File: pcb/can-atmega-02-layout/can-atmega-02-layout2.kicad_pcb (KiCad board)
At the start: 2 copper layers, 114 x 98 mm, 168 parts, among them J1 Screw_Terminal_01x05, J3 Conn_02x03_Odd_Even, J4 Connector_female, U1 LM1117-5.0, U2 TJA1051T, U3 MCP2515-xSO, U4 ATmega328P-A, X1 16MHz, X2 16MHz

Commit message: temp-calibrate
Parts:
- removed the C1 at (107.9, 33.1)
- removed the C1 at (69.9, 82.1)
- removed the C1 at (69.9, 33.1)
- removed the C1 at (31.9, 82.1)
- removed the C1 at (107.9, 82.1)
- removed the C1 at (31.9, 33.1)
- removed C10 (x6), C11 (x6), C5 (x6), C6 (x6): 22PF, Capacitor_SMD:C_1206_3216Metric
- removed the C2 at (71.0, 37.9)
- removed the C2 at (33.0, 37.9)
- removed the C2 at (109.0, 37.9)
- removed the C2 at (71.0, 86.9)
- removed the C2 at (109.0, 86.9)
- removed the C2 at (33.0, 86.9)
- removed the C3 at (112.3, 37.9)
- removed the C3 at (36.3, 37.9)
- removed the C3 at (112.3, 86.9)
- removed the C3 at (74.3, 37.9)
- removed the C3 at (36.3, 86.9)
- removed the C3 at (74.3, 86.9)
- removed the C4 at (77.6, 37.9)
- removed the C4 at (39.6, 37.9)
- removed the C4 at (39.6, 86.9)
- removed the C4 at (115.6, 86.9)
- removed the C4 at (115.6, 37.9)
- removed the C4 at (77.6, 86.9)
- removed C7 (x6), C9 (x6): 0.1uF, Capacitor_SMD:C_1206_3216Metric
- removed C8 (x6): 10uF/16V, Capacitor_SMD:C_1206_3216Metric
- removed the J1 at (32.6, 74.7)
- removed the J1 at (32.6, 25.7)
- removed the J1 at (70.6, 25.7)
- removed the J1 at (70.6, 74.7)
- removed the J1 at (108.6, 74.7)
- removed the J1 at (108.6, 25.7)
- removed J3 (x6): Conn_02x03_Odd_Even, Connector_IDC:IDC-Header_2x03_P2.54mm_Vertical
- removed J4 (x6): Connector_female, CAN_ATmega:Connector_female
- removed LED1 (x6): Green, LED_SMD:LED_0805_2012Metric
- removed R1 (x6): 1K, Resistor_SMD:R_0805_2012Metric
- removed R2 (x6): 10K, Resistor_SMD:R_0805_2012Metric
- removed the R3 at (75.6, 99.2)
- removed the R3 at (75.6, 50.2)
- removed the R3 at (37.6, 50.2)
- removed the R3 at (37.6, 99.2)
- removed the R3 at (113.6, 99.2)
- removed the R3 at (113.6, 50.2)
- removed the REF** at (48.5, 16.5)
- removed the REF** at (54.5, 59.5)
- removed the REF** at (54.5, 65.5)
- removed the REF** at (86.5, 108.5)
- removed the REF** at (92.5, 65.5)
- removed the REF** at (16.5, 108.5)
- removed the REF** at (16.5, 65.5)
- removed the REF** at (86.5, 16.5)
- removed the REF** at (92.5, 16.5)
- removed the REF** at (48.5, 65.5)
- removed the REF** at (124.5, 16.5)
- removed the REF** at (124.5, 65.5)
- removed the REF** at (124.5, 59.5)
- removed the REF** at (92.5, 59.5)
- removed the REF** at (48.5, 108.5)
- removed the REF** at (124.5, 108.5)
- removed the REF** at (48.5, 59.5)
- removed the REF** at (54.5, 16.5)
- removed the REF** at (92.5, 108.5)
- removed the REF** at (86.5, 65.5)
- removed the REF** at (16.5, 59.5)
- removed the REF** at (16.5, 16.5)
- removed the REF** at (86.5, 59.5)
- removed the REF** at (54.5, 108.5)
- removed the U1 at (75.8, 80.8)
- removed the U1 at (37.8, 31.8)
- removed the U1 at (113.8, 80.8)
- removed the U1 at (75.8, 31.8)
- removed the U1 at (113.8, 31.8)
- removed the U1 at (37.8, 80.8)
- removed U2 (x6): TJA1051T, Package_SO:SOIC-8_3.9x4.9mm_P1.27mm
- removed U3 (x6): MCP2515-xSO, Package_SO:SOIC-18W_7.5x11.6mm_P1.27mm
- removed U4 (x6): ATmega328P-A, Package_QFP:TQFP-32_7x7mm_P0.8mm
- removed X1 (x6), X2 (x6): 16MHz, Crystal:Crystal_HC49-4H_Vertical
- added C1: 100nF, Capacitor_SMD:C_1206_3216Metric, B.Cu at (22.0, 23.3)
- added C1: 100nF, Capacitor_SMD:C_1206_3216Metric, B.Cu at (22.0, 51.3)
- added C1: 100nF, Capacitor_SMD:C_1206_3216Metric, B.Cu at (98.0, 23.3)
- added C1: 100nF, Capacitor_SMD:C_1206_3216Metric, B.Cu at (60.0, 51.3)
- added C1: 100nF, Capacitor_SMD:C_1206_3216Metric, B.Cu at (60.0, 23.3)
- added C1: 100nF, Capacitor_SMD:C_1206_3216Metric, B.Cu at (98.0, 51.3)
- added C2: 100nF, Capacitor_SMD:C_1206_3216Metric, B.Cu at (98.0, 54.6)
- added C2: 100nF, Capacitor_SMD:C_1206_3216Metric, B.Cu at (98.0, 26.6)
- added C2: 100nF, Capacitor_SMD:C_1206_3216Metric, B.Cu at (22.0, 54.6)
- added C2: 100nF, Capacitor_SMD:C_1206_3216Metric, B.Cu at (60.0, 26.6)
- added C2: 100nF, Capacitor_SMD:C_1206_3216Metric, B.Cu at (22.0, 26.6)
- added C2: 100nF, Capacitor_SMD:C_1206_3216Metric, B.Cu at (60.0, 54.6)
- added C3: 10uF/16V, Capacitor_SMD:C_1206_3216Metric, B.Cu at (60.0, 57.6)
- added C3: 10uF/16V, Capacitor_SMD:C_1206_3216Metric, B.Cu at (22.0, 57.6)
- added C3: 10uF/16V, Capacitor_SMD:C_1206_3216Metric, B.Cu at (60.0, 29.6)
- added C3: 10uF/16V, Capacitor_SMD:C_1206_3216Metric, B.Cu at (98.0, 29.6)
- added C3: 10uF/16V, Capacitor_SMD:C_1206_3216Metric, B.Cu at (22.0, 29.6)
- added C3: 10uF/16V, Capacitor_SMD:C_1206_3216Metric, B.Cu at (98.0, 57.6)
- added C4: 100nF, Capacitor_SMD:C_1206_3216Metric, B.Cu at (119.4, 51.3)
- added C4: 100nF, Capacitor_SMD:C_1206_3216Metric, B.Cu at (81.4, 51.3)
- added C4: 100nF, Capacitor_SMD:C_1206_3216Metric, B.Cu at (81.4, 23.3)
- added C4: 100nF, Capacitor_SMD:C_1206_3216Metric, B.Cu at (43.4, 51.3)
- added C4: 100nF, Capacitor_SMD:C_1206_3216Metric, B.Cu at (119.4, 23.3)
- added C4: 100nF, Capacitor_SMD:C_1206_3216Metric, B.Cu at (43.4, 23.3)
- added J1: Connector_male, CAN_ATmega:Connector_male, F.Cu at (107.2, 23.3)
- added J1: Connector_male, CAN_ATmega:Connector_male, F.Cu at (31.2, 51.3)
- added J1: Connector_male, CAN_ATmega:Connector_male, F.Cu at (69.2, 23.3)
- added J1: Connector_male, CAN_ATmega:Connector_male, F.Cu at (107.2, 51.3)
- added J1: Connector_male, CAN_ATmega:Connector_male, F.Cu at (69.2, 51.3)
- added J1: Connector_male, CAN_ATmega:Connector_male, F.Cu at (31.2, 23.3)
- added J2: Screw_Terminal_01x03, Connector_Wago:Wago_734-163_1x03_P3.50mm_Horizontal, F.Cu at (66.8, 32.5)
- added J2: Screw_Terminal_01x03, Connector_Wago:Wago_734-163_1x03_P3.50mm_Horizontal, F.Cu at (28.8, 32.5)
- added J2: Screw_Terminal_01x03, Connector_Wago:Wago_734-163_1x03_P3.50mm_Horizontal, F.Cu at (104.8, 60.5)
- added J2: Screw_Terminal_01x03, Connector_Wago:Wago_734-163_1x03_P3.50mm_Horizontal, F.Cu at (66.8, 60.5)
- added J2: Screw_Terminal_01x03, Connector_Wago:Wago_734-163_1x03_P3.50mm_Horizontal, F.Cu at (104.8, 32.5)
- added J2: Screw_Terminal_01x03, Connector_Wago:Wago_734-163_1x03_P3.50mm_Horizontal, F.Cu at (28.8, 60.5)
- added R1_1: 1.3k, Resistor_SMD:R_0805_2012Metric, F.Cu at (101.6, 18.7)
- added R1_1: 1.3k, Resistor_SMD:R_0805_2012Metric, F.Cu at (101.6, 46.7)
- added R1_1: 1.3k, Resistor_SMD:R_0805_2012Metric, F.Cu at (63.6, 46.7)
- added R1_1: 1.3k, Resistor_SMD:R_0805_2012Metric, F.Cu at (25.6, 46.7)
- added R1_1: 1.3k, Resistor_SMD:R_0805_2012Metric, F.Cu at (25.6, 18.7)
- added R1_1: 1.3k, Resistor_SMD:R_0805_2012Metric, F.Cu at (63.6, 18.7)
- added R1_2: 2k, Resistor_SMD:R_0805_2012Metric, F.Cu at (60.8, 47.7)
- added R1_2: 2k, Resistor_SMD:R_0805_2012Metric, F.Cu at (22.8, 47.7)
- added R1_2: 2k, Resistor_SMD:R_0805_2012Metric, F.Cu at (22.8, 19.7)
- added R1_2: 2k, Resistor_SMD:R_0805_2012Metric, F.Cu at (98.8, 47.7)
- added R1_2: 2k, Resistor_SMD:R_0805_2012Metric, F.Cu at (98.8, 19.7)
- added R1_2: 2k, Resistor_SMD:R_0805_2012Metric, F.Cu at (60.8, 19.7)
- added R1_3: 10k, Resistor_SMD:R_0805_2012Metric, F.Cu at (63.6, 20.7)
- added R1_3: 10k, Resistor_SMD:R_0805_2012Metric, F.Cu at (101.6, 48.7)
- added R1_3: 10k, Resistor_SMD:R_0805_2012Metric, F.Cu at (25.6, 20.7)
- added R1_3: 10k, Resistor_SMD:R_0805_2012Metric, F.Cu at (101.6, 20.7)
- added R1_3: 10k, Resistor_SMD:R_0805_2012Metric, F.Cu at (63.6, 48.7)
- added R1_3: 10k, Resistor_SMD:R_0805_2012Metric, F.Cu at (25.6, 48.7)
- added R2_1: 330, Resistor_SMD:R_0805_2012Metric, F.Cu at (115.3, 23.0)
- added R2_1: 330, Resistor_SMD:R_0805_2012Metric, F.Cu at (77.3, 23.0)
- added R2_1: 330, Resistor_SMD:R_0805_2012Metric, F.Cu at (39.3, 23.0)
- added R2_1: 330, Resistor_SMD:R_0805_2012Metric, F.Cu at (115.3, 51.0)
- added R2_1: 330, Resistor_SMD:R_0805_2012Metric, F.Cu at (39.3, 51.0)
- added R2_1: 330, Resistor_SMD:R_0805_2012Metric, F.Cu at (77.3, 51.0)
- added R2_2: 1.3k, Resistor_SMD:R_0805_2012Metric, F.Cu at (42.1, 22.0)
- added R2_2: 1.3k, Resistor_SMD:R_0805_2012Metric, F.Cu at (80.1, 22.0)
- added R2_2: 1.3k, Resistor_SMD:R_0805_2012Metric, F.Cu at (118.1, 22.0)
- added R2_2: 1.3k, Resistor_SMD:R_0805_2012Metric, F.Cu at (80.1, 50.0)
- added R2_2: 1.3k, Resistor_SMD:R_0805_2012Metric, F.Cu at (118.1, 50.0)
- added R2_2: 1.3k, Resistor_SMD:R_0805_2012Metric, F.Cu at (42.1, 50.0)
- added R2_3: 110k, Resistor_SMD:R_0805_2012Metric, F.Cu at (77.3, 21.0)
- added R2_3: 110k, Resistor_SMD:R_0805_2012Metric, F.Cu at (39.3, 21.0)
- added R2_3: 110k, Resistor_SMD:R_0805_2012Metric, F.Cu at (39.3, 49.0)
- added R2_3: 110k, Resistor_SMD:R_0805_2012Metric, F.Cu at (77.3, 49.0)
- added R2_3: 110k, Resistor_SMD:R_0805_2012Metric, F.Cu at (115.3, 21.0)
- added R2_3: 110k, Resistor_SMD:R_0805_2012Metric, F.Cu at (115.3, 49.0)
- added R3: 20k, Resistor_SMD:R_0805_2012Metric, F.Cu at (81.5, 44.0)
- added R3: 20k, Resistor_SMD:R_0805_2012Metric, F.Cu at (119.5, 16.0)
- added R3: 20k, Resistor_SMD:R_0805_2012Metric, F.Cu at (43.5, 16.0)
- added R3: 20k, Resistor_SMD:R_0805_2012Metric, F.Cu at (81.5, 16.0)
- added R3: 20k, Resistor_SMD:R_0805_2012Metric, F.Cu at (119.5, 44.0)
- added R3: 20k, Resistor_SMD:R_0805_2012Metric, F.Cu at (43.5, 44.0)
- added R4_1: 2k, Resistor_SMD:R_0805_2012Metric, F.Cu at (57.6, 32.0)
- added R4_1: 2k, Resistor_SMD:R_0805_2012Metric, F.Cu at (19.6, 32.0)
- added R4_1: 2k, Resistor_SMD:R_0805_2012Metric, F.Cu at (95.6, 60.0)
- added R4_1: 2k, Resistor_SMD:R_0805_2012Metric, F.Cu at (57.6, 60.0)
- added R4_1: 2k, Resistor_SMD:R_0805_2012Metric, F.Cu at (95.6, 32.0)
- added R4_1: 2k, Resistor_SMD:R_0805_2012Metric, F.Cu at (19.6, 60.0)
- added R4_2: 2.4k, Resistor_SMD:R_0805_2012Metric, F.Cu at (20.6, 34.8)
- added R4_2: 2.4k, Resistor_SMD:R_0805_2012Metric, F.Cu at (96.6, 62.8)
- added R4_2: 2.4k, Resistor_SMD:R_0805_2012Metric, F.Cu at (58.6, 34.8)
- added R4_2: 2.4k, Resistor_SMD:R_0805_2012Metric, F.Cu at (20.6, 62.8)
- added R4_2: 2.4k, Resistor_SMD:R_0805_2012Metric, F.Cu at (58.6, 62.8)
- added R4_2: 2.4k, Resistor_SMD:R_0805_2012Metric, F.Cu at (96.6, 34.8)
- added R4_3: 20k, Resistor_SMD:R_0805_2012Metric, F.Cu at (97.6, 32.0)
- added R4_3: 20k, Resistor_SMD:R_0805_2012Metric, F.Cu at (21.6, 60.0)
- added R4_3: 20k, Resistor_SMD:R_0805_2012Metric, F.Cu at (59.6, 32.0)
- added R4_3: 20k, Resistor_SMD:R_0805_2012Metric, F.Cu at (21.6, 32.0)
- added R4_3: 20k, Resistor_SMD:R_0805_2012Metric, F.Cu at (97.6, 60.0)
- added R4_3: 20k, Resistor_SMD:R_0805_2012Metric, F.Cu at (59.6, 60.0)
- added R5: 1k, Resistor_SMD:R_0805_2012Metric, F.Cu at (43.1, 33.4)
- added R5: 1k, Resistor_SMD:R_0805_2012Metric, F.Cu at (119.1, 61.4)
- added R5: 1k, Resistor_SMD:R_0805_2012Metric, F.Cu at (119.1, 33.4)
- added R5: 1k, Resistor_SMD:R_0805_2012Metric, F.Cu at (81.1, 33.4)
- added R5: 1k, Resistor_SMD:R_0805_2012Metric, F.Cu at (43.1, 61.4)
- added R5: 1k, Resistor_SMD:R_0805_2012Metric, F.Cu at (81.1, 61.4)
- added REF**: MountingHole_2.2mm_M2, MountingHole:MountingHole_2.2mm_M2, F.Cu at (92.5, 66.5)
- added REF**: MountingHole_2.2mm_M2, MountingHole:MountingHole_2.2mm_M2, F.Cu at (124.5, 38.5)
- added REF**: MountingHole_2.2mm_M2, MountingHole:MountingHole_2.2mm_M2, F.Cu at (54.5, 66.5)
- added REF**: MountingHole_2.2mm_M2, MountingHole:MountingHole_2.2mm_M2, F.Cu at (92.5, 38.5)
- added REF**: MountingHole_2.2mm_M2, MountingHole:MountingHole_2.2mm_M2, F.Cu at (16.5, 66.5)
- added REF**: MountingHole_2.2mm_M2, MountingHole:MountingHole_2.2mm_M2, F.Cu at (54.5, 38.5)
- added REF**: MountingHole_2.2mm_M2, MountingHole:MountingHole_2.2mm_M2, F.Cu at (48.5, 38.5)
- added REF**: MountingHole_2.2mm_M2, MountingHole:MountingHole_2.2mm_M2, F.Cu at (86.5, 38.5)
- added REF**: MountingHole_2.2mm_M2, MountingHole:MountingHole_2.2mm_M2, F.Cu at (86.5, 66.5)
- added REF**: MountingHole_2.2mm_M2, MountingHole:MountingHole_2.2mm_M2, F.Cu at (16.5, 38.5)
- added REF**: MountingHole_2.2mm_M2, MountingHole:MountingHole_2.2mm_M2, F.Cu at (124.5, 66.5)
- added REF**: MountingHole_2.2mm_M2, MountingHole:MountingHole_2.2mm_M2, F.Cu at (48.5, 66.5)
- added U1: MCP6002-xP, Package_DIP:DIP-8_W7.62mm, F.Cu at (28.6, 46.2)
- added U1: MCP6002-xP, Package_DIP:DIP-8_W7.62mm, F.Cu at (104.6, 18.2)
- added U1: MCP6002-xP, Package_DIP:DIP-8_W7.62mm, F.Cu at (66.6, 18.2)
- added U1: MCP6002-xP, Package_DIP:DIP-8_W7.62mm, F.Cu at (66.6, 46.2)
- added U1: MCP6002-xP, Package_DIP:DIP-8_W7.62mm, F.Cu at (28.6, 18.2)
- added U1: MCP6002-xP, Package_DIP:DIP-8_W7.62mm, F.Cu at (104.6, 46.2)
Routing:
- net +5V: track 922.4 -> 398.4 mm, vias 18 -> 6
- net GND: track 554.3 -> 98.5 mm, vias 90 -> 24
- net U4_RST: track 305.2 -> 0.00 mm, vias 12 -> 0
- net U4_D11_MOSI: track 300.0 -> 0.00 mm, vias 18 -> 0
- net U4_D13_SCK: track 295.2 -> 0.00 mm, vias 12 -> 0
- net U4_D12_MISO: track 279.1 -> 0.00 mm, vias 12 -> 0
- net /vk_in: track 0.00 -> 257.0 mm
- net +12V: track 195.7 -> 0.00 mm
- net U4_D4: track 176.6 -> 0.00 mm
- net U4_D3: track 173.6 -> 0.00 mm
- net U4_D6: track 123.8 -> 0.00 mm
- net U4_D5: track 118.3 -> 0.00 mm
- net CAN_H: track 113.7 -> 0.00 mm
- net /S2: track 0.00 -> 112.4 mm
- net D10_CS: track 112.4 -> 0.00 mm, vias 12 -> 0
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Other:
- board size 114 x 98 mm -> 114 x 56 mm
- board text added: "GND"
- board text added: "R1"
- board text added: "R2"
- board text added: "R4"
- board text added: "Sensor"

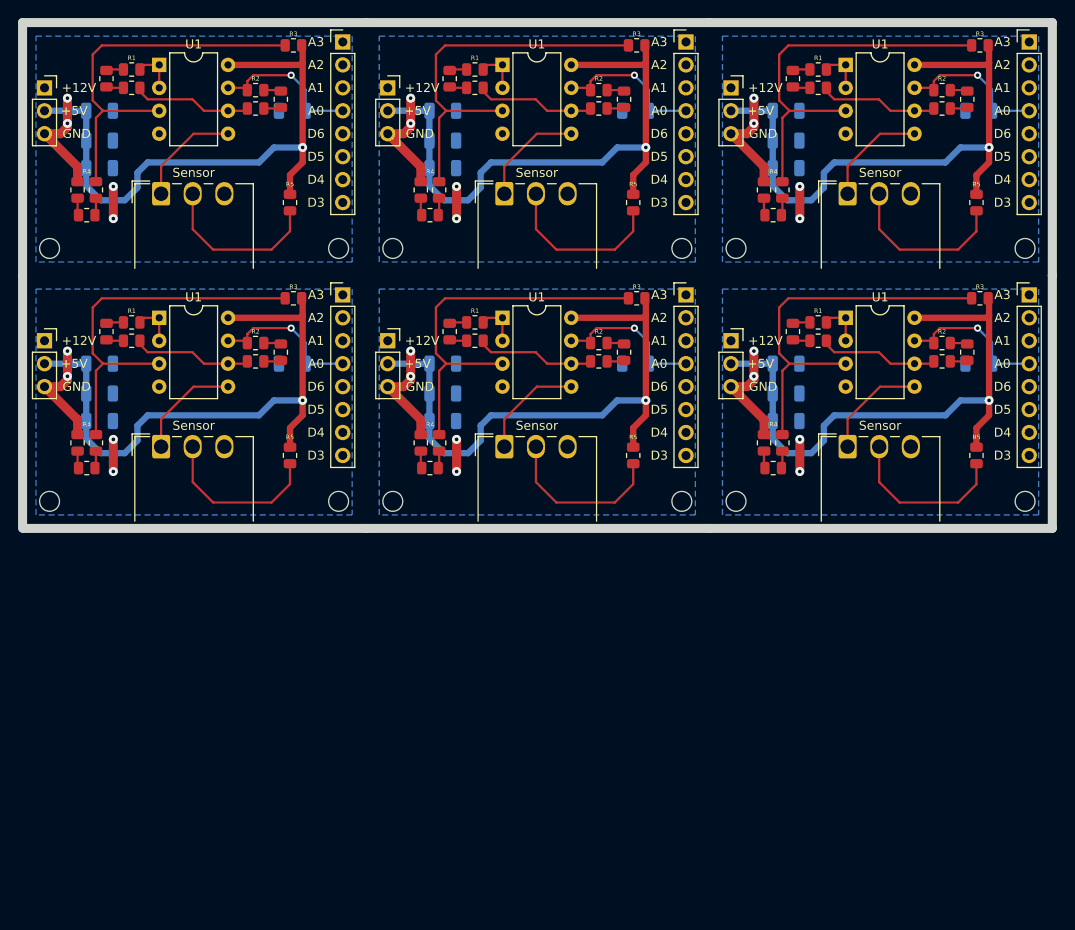
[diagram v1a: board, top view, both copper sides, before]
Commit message: new temp module
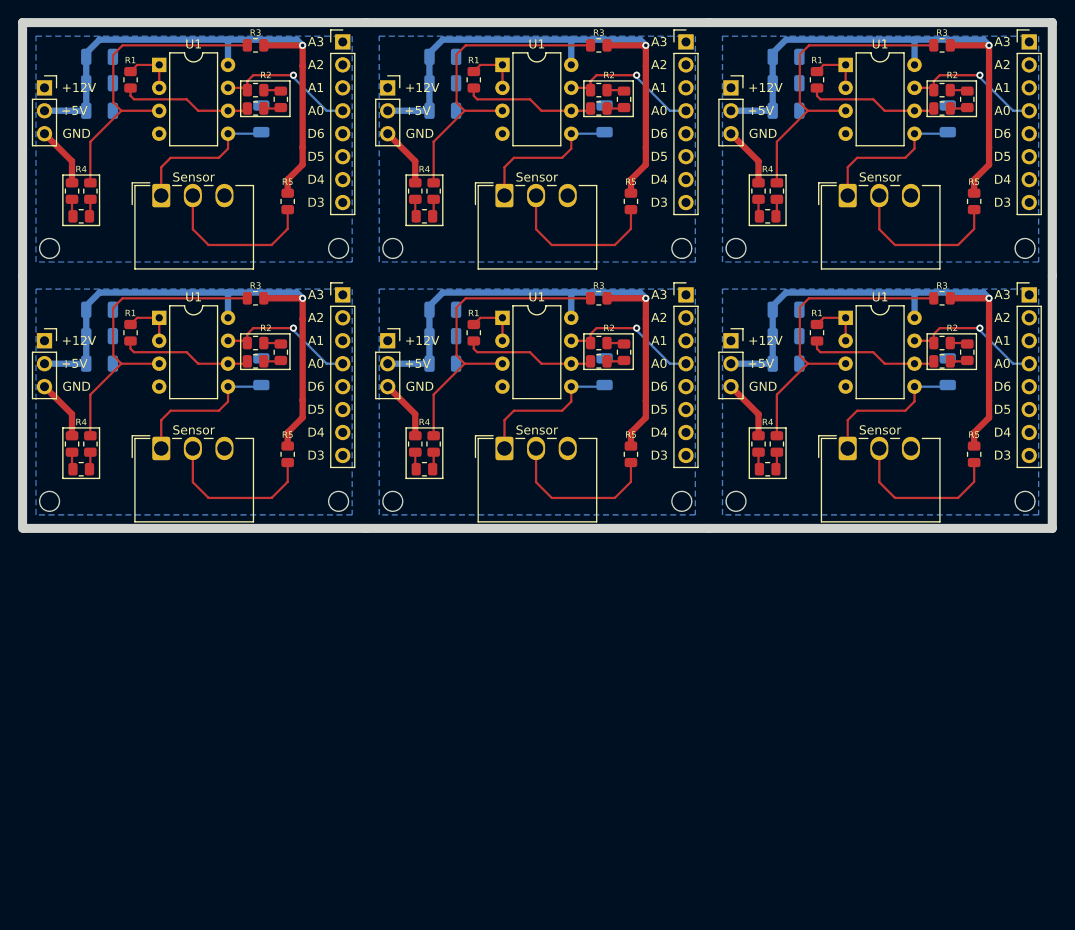
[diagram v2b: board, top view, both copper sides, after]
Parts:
- removed the C2 at (98.0, 54.6)
- removed the C2 at (98.0, 26.6)
- removed the C2 at (22.0, 54.6)
- removed the C2 at (60.0, 26.6)
- removed the C2 at (22.0, 26.6)
- removed the C2 at (60.0, 54.6)
- removed the C3 at (60.0, 57.6)
- removed the C3 at (22.0, 57.6)
- removed the C3 at (60.0, 29.6)
- removed the C3 at (98.0, 29.6)
- removed the C3 at (22.0, 29.6)
- removed the C3 at (98.0, 57.6)
- removed the C4 at (119.4, 51.3)
- removed the C4 at (81.4, 51.3)
- removed the C4 at (81.4, 23.3)
- removed the C4 at (43.4, 51.3)
- removed the C4 at (119.4, 23.3)
- removed the C4 at (43.4, 23.3)
- removed the J2 at (66.8, 32.5)
- removed the J2 at (28.8, 32.5)
- removed the J2 at (104.8, 60.5)
- removed the J2 at (66.8, 60.5)
- removed the J2 at (104.8, 32.5)
- removed the J2 at (28.8, 60.5)
- removed R1_1 (x6): 1.3k, Resistor_SMD:R_0805_2012Metric
- removed R1_2 (x6): 2k, Resistor_SMD:R_0805_2012Metric
- removed R1_3 (x6): 10k, Resistor_SMD:R_0805_2012Metric
- removed the R3 at (81.5, 44.0)
- removed the R3 at (119.5, 16.0)
- removed the R3 at (43.5, 16.0)
- removed the R3 at (81.5, 16.0)
- removed the R3 at (119.5, 44.0)
- removed the R3 at (43.5, 44.0)
- removed the R4_1 at (57.6, 32.0)
- removed the R4_1 at (19.6, 32.0)
- removed the R4_1 at (95.6, 60.0)
- removed the R4_1 at (57.6, 60.0)
- removed the R4_1 at (95.6, 32.0)
- removed the R4_1 at (19.6, 60.0)
- removed the R4_2 at (20.6, 34.8)
- removed the R4_2 at (96.6, 62.8)
- removed the R4_2 at (58.6, 34.8)
- removed the R4_2 at (20.6, 62.8)
- removed the R4_2 at (58.6, 62.8)
- removed the R4_2 at (96.6, 34.8)
- removed the R4_3 at (97.6, 32.0)
- removed the R4_3 at (21.6, 60.0)
- removed the R4_3 at (59.6, 32.0)
- removed the R4_3 at (21.6, 32.0)
- removed the R4_3 at (97.6, 60.0)
- removed the R4_3 at (59.6, 60.0)
- removed the R5 at (43.1, 33.4)
- removed the R5 at (119.1, 61.4)
- removed the R5 at (119.1, 33.4)
- removed the R5 at (81.1, 33.4)
- removed the R5 at (43.1, 61.4)
- removed the R5 at (81.1, 61.4)
- added C2: 100nF, Capacitor_SMD:C_1206_3216Metric, B.Cu at (60.0, 48.2)
- added C2: 100nF, Capacitor_SMD:C_1206_3216Metric, B.Cu at (98.0, 20.2)
- added C2: 100nF, Capacitor_SMD:C_1206_3216Metric, B.Cu at (22.0, 48.2)
- added C2: 100nF, Capacitor_SMD:C_1206_3216Metric, B.Cu at (60.0, 20.2)
- added C2: 100nF, Capacitor_SMD:C_1206_3216Metric, B.Cu at (22.0, 20.2)
- added C2: 100nF, Capacitor_SMD:C_1206_3216Metric, B.Cu at (98.0, 48.2)
- added C3: 10uF/16V, Capacitor_SMD:C_1206_3216Metric, B.Cu at (60.0, 45.3)
- added C3: 10uF/16V, Capacitor_SMD:C_1206_3216Metric, B.Cu at (22.0, 17.3)
- added C3: 10uF/16V, Capacitor_SMD:C_1206_3216Metric, B.Cu at (22.0, 45.3)
- added C3: 10uF/16V, Capacitor_SMD:C_1206_3216Metric, B.Cu at (60.0, 17.3)
- added C3: 10uF/16V, Capacitor_SMD:C_1206_3216Metric, B.Cu at (98.0, 45.3)
- added C3: 10uF/16V, Capacitor_SMD:C_1206_3216Metric, B.Cu at (98.0, 17.3)
- added C4: 100nF, Capacitor_SMD:C_1206_3216Metric, B.Cu at (115.9, 24.2)
- added C4: 100nF, Capacitor_SMD:C_1206_3216Metric, B.Cu at (77.9, 24.2)
- added C4: 100nF, Capacitor_SMD:C_1206_3216Metric, B.Cu at (77.9, 52.2)
- added C4: 100nF, Capacitor_SMD:C_1206_3216Metric, B.Cu at (39.9, 24.2)
- added C4: 100nF, Capacitor_SMD:C_1206_3216Metric, B.Cu at (39.9, 52.2)
- added C4: 100nF, Capacitor_SMD:C_1206_3216Metric, B.Cu at (115.9, 52.2)
- added J2: Screw_Terminal_01x03, Connector_Wago:Wago_734-163_1x03_P3.50mm_Horizontal, F.Cu at (104.9, 60.7)
- added J2: Screw_Terminal_01x03, Connector_Wago:Wago_734-163_1x03_P3.50mm_Horizontal, F.Cu at (66.9, 32.7)
- added J2: Screw_Terminal_01x03, Connector_Wago:Wago_734-163_1x03_P3.50mm_Horizontal, F.Cu at (28.9, 32.7)
- added J2: Screw_Terminal_01x03, Connector_Wago:Wago_734-163_1x03_P3.50mm_Horizontal, F.Cu at (28.9, 60.7)
- added J2: Screw_Terminal_01x03, Connector_Wago:Wago_734-163_1x03_P3.50mm_Horizontal, F.Cu at (104.9, 32.7)
- added J2: Screw_Terminal_01x03, Connector_Wago:Wago_734-163_1x03_P3.50mm_Horizontal, F.Cu at (66.9, 60.7)
- added R1: 10k, Resistor_SMD:R_0805_2012Metric, F.Cu at (101.5, 47.8)
- added R1: 10k, Resistor_SMD:R_0805_2012Metric, F.Cu at (63.5, 47.8)
- added R1: 10k, Resistor_SMD:R_0805_2012Metric, F.Cu at (25.5, 19.8)
- added R1: 10k, Resistor_SMD:R_0805_2012Metric, F.Cu at (25.5, 47.8)
- added R1: 10k, Resistor_SMD:R_0805_2012Metric, F.Cu at (63.5, 19.8)
- added R1: 10k, Resistor_SMD:R_0805_2012Metric, F.Cu at (101.5, 19.8)
- added R3: 20.5k, Resistor_SMD:R_0805_2012Metric, F.Cu at (115.3, 44.0)
- added R3: 20.5k, Resistor_SMD:R_0805_2012Metric, F.Cu at (77.3, 16.0)
- added R3: 20.5k, Resistor_SMD:R_0805_2012Metric, F.Cu at (115.3, 16.0)
- added R3: 20.5k, Resistor_SMD:R_0805_2012Metric, F.Cu at (39.3, 44.0)
- added R3: 20.5k, Resistor_SMD:R_0805_2012Metric, F.Cu at (77.3, 44.0)
- added R3: 20.5k, Resistor_SMD:R_0805_2012Metric, F.Cu at (39.3, 16.0)
- added R4_1: 3k, Resistor_SMD:R_0805_2012Metric, F.Cu at (57.0, 60.2)
- added R4_1: 3k, Resistor_SMD:R_0805_2012Metric, F.Cu at (95.0, 60.2)
- added R4_1: 3k, Resistor_SMD:R_0805_2012Metric, F.Cu at (57.0, 32.2)
- added R4_1: 3k, Resistor_SMD:R_0805_2012Metric, F.Cu at (19.0, 60.2)
- added R4_1: 3k, Resistor_SMD:R_0805_2012Metric, F.Cu at (95.0, 32.2)
- added R4_1: 3k, Resistor_SMD:R_0805_2012Metric, F.Cu at (19.0, 32.2)
- added R4_2: 3k, Resistor_SMD:R_0805_2012Metric, F.Cu at (96.0, 62.9)
- added R4_2: 3k, Resistor_SMD:R_0805_2012Metric, F.Cu at (58.0, 62.9)
- added R4_2: 3k, Resistor_SMD:R_0805_2012Metric, F.Cu at (20.0, 62.9)
- added R4_2: 3k, Resistor_SMD:R_0805_2012Metric, F.Cu at (96.0, 34.9)
- added R4_2: 3k, Resistor_SMD:R_0805_2012Metric, F.Cu at (20.0, 34.9)
- added R4_2: 3k, Resistor_SMD:R_0805_2012Metric, F.Cu at (58.0, 34.9)
- added R4_3: 1k, Resistor_SMD:R_0805_2012Metric, F.Cu at (59.0, 32.2)
- added R4_3: 1k, Resistor_SMD:R_0805_2012Metric, F.Cu at (21.0, 32.2)
- added R4_3: 1k, Resistor_SMD:R_0805_2012Metric, F.Cu at (21.0, 60.2)
- added R4_3: 1k, Resistor_SMD:R_0805_2012Metric, F.Cu at (97.0, 32.2)
- added R4_3: 1k, Resistor_SMD:R_0805_2012Metric, F.Cu at (59.0, 60.2)
- added R4_3: 1k, Resistor_SMD:R_0805_2012Metric, F.Cu at (97.0, 60.2)
- added R5: 3k, Resistor_SMD:R_0805_2012Metric, F.Cu at (118.9, 33.3)
- added R5: 3k, Resistor_SMD:R_0805_2012Metric, F.Cu at (80.9, 33.3)
- added R5: 3k, Resistor_SMD:R_0805_2012Metric, F.Cu at (42.9, 61.3)
- added R5: 3k, Resistor_SMD:R_0805_2012Metric, F.Cu at (118.9, 61.3)
- added R5: 3k, Resistor_SMD:R_0805_2012Metric, F.Cu at (42.9, 33.3)
- added R5: 3k, Resistor_SMD:R_0805_2012Metric, F.Cu at (80.9, 61.3)
- R2_1 (x6): value 330 -> 20.5k
- R2_2 (x6): value 1.3k -> 20.5k
- R2_3 (x6): value 110k -> 10k
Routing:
- net GND: track 98.5 -> 40.2 mm, vias 24 -> 0
- net /vk_in: track 257.0 -> 212.6 mm
- net +5V: track 398.4 -> 360.2 mm
- net S1: track 71.7 -> 100.7 mm
- net /R_1_1_2: track 11.5 -> 0.00 mm
- net /R_1_2_3: track 11.5 -> 0.00 mm
- net /fb: track 79.7 -> 87.5 mm
- net SREG: track 102.4 -> 95.1 mm
- net /vk_buf: track 29.3 -> 36.1 mm
- net /S2: track 112.4 -> 107.0 mm
- net /R_4_2_3: track 12.4 -> 11.5 mm
- net /R_4_1_2: track 12.4 -> 11.5 mm
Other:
- board text removed: "R1"
